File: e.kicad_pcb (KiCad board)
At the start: 2 copper layers, 78 x 58.5 mm, 9 parts, among them SW1 usr, SW2 rst, U1 Display_ST7789, U2 MAX98357A

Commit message: final changes, yay!
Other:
- board size 78 x 58.5 mm -> 78 x 58.3 mm
- board text added: "from monty X3"
- board text added: "text here"
- board text removed: "made by montypythonist X3"
- board text removed: "some notes: insert words here :)"
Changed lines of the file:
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@@
 		(at 166.45 98.31 90)
 		(property "Reference" "U1"
-			(at 0 -1.6 90)
+			(at -23.19 19.55 0)
 			(unlocked yes)
 			(layer "F.SilkS")
@@
 		(attr smd)
 		(duplicate_pad_numbers_are_jumpers no)
-		(fp_rect
-			(start -21.85 -21)
-			(end 21.85 20.8)
+		(fp_line
+			(start 21.844 -21)
+			(end 21.336 -21)
 			(stroke
 				(width 0.1)
-				(type solid)
+				(type default)
+			)
+			(layer "F.SilkS")
+		)
+		(fp_line
+			(start 21.844 -21)
+			(end 21.844 -20.492)
+			(stroke
+				(width 0.1)
+				(type default)
+			)
+			(layer "F.SilkS")
+		)
+		(fp_line
+			(start -21.844 20.828)
+			(end -21.844 20.32)
+			(stroke
+				(width 0.1)
+				(type default)
+			)
+			(layer "F.SilkS")
+		)
+		(fp_line
+			(start -21.844 20.828)
+			(end -21.336 20.828)
+			(stroke
+				(width 0.1)
+				(type default)
 			)
-			(fill no)
 			(layer "F.SilkS")
 		)
@@
 		(at 127.65 88.35 90)
 		(property "Reference" "LS1"
-			(at 14.7 -7 180)
+			(at 12.85 10.85 90)
 			(unlocked yes)
 			(layer "F.SilkS")
@@
 	(gr_rect
 		(start 112.15 66.15)
-		(end 190.15 124.650001)
+		(end 190.15 124.499999)
 		(stroke
 			(width 0.05)
@@
 	)
 	(gr_text "this routing haunts me in my sleep"
-		(at 189.15 109.65 90)
+		(at 188.5 111 90)
 		(layer "F.SilkS")
 		(effects
 			(font
-				(size 0.5 0.5)
+				(size 0.7 0.7)
 				(thickness 0.1)
 				(bold yes)
@@
 	)
 	(gr_text "on"
-		(at 135.649999 70.473333 90)
+		(at 136 71 90)
 		(layer "F.SilkS")
 		(effects
 			(font
-				(size 0.7 0.7)
+				(size 0.8 0.8)
 				(thickness 0.1)
 				(bold yes)
@@
 	)
 	(gr_text "off"
-		(at 122.649999 69.473333 270)
+		(at 122 69.5 270)
 		(layer "F.SilkS")
 		(effects
 			(font
-				(size 0.7 0.7)
+				(size 0.8 0.8)
 				(thickness 0.1)
 				(bold yes)
@@
 		)
 	)
-	(gr_text "made by\nmontypythonist X3"
-		(at 113.65 74.15 270)
+	(gr_text "from monty X3"
+		(at 113.5 67.5 270)
 		(layer "F.SilkS")
 		(effects
@@
 				(thickness 0.1)
 			)
-			(justify bottom)
+			(justify left bottom)
 		)
 	)
-	(gr_text "some notes: \ninsert words here :)"
+	(gr_text "text here"
 		(at 117.15 123.65 90)
 		(layer "F.SilkS")
@@
 		)
 	)
-	(group ""
-		(members "b0904ed2-5f99-419c-b382-4dc33d7675e0")
-	)
-	(group ""
-		(members "44044c4c-9110-4a88-b0ce-294c61a6f578")
-	)
-	(group ""
-		(members "03bbb989-da97-4d1e-8210-7c8b60939a85" "ce20f35f-f039-4fc7-9ab9-af98ebee2966")
-	)
 	(embedded_fonts no)

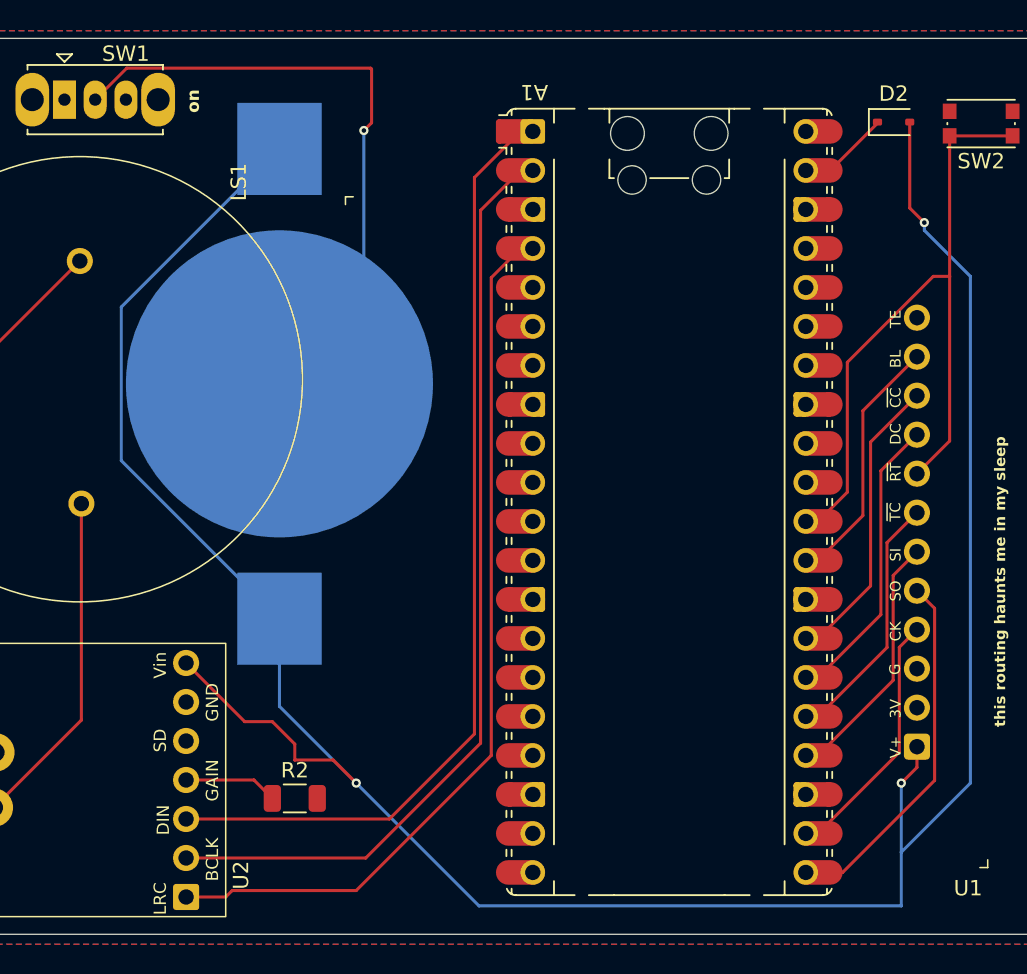
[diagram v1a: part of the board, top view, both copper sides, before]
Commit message: minor schematic cosmetic changes, cleaned up a few traces on PCB
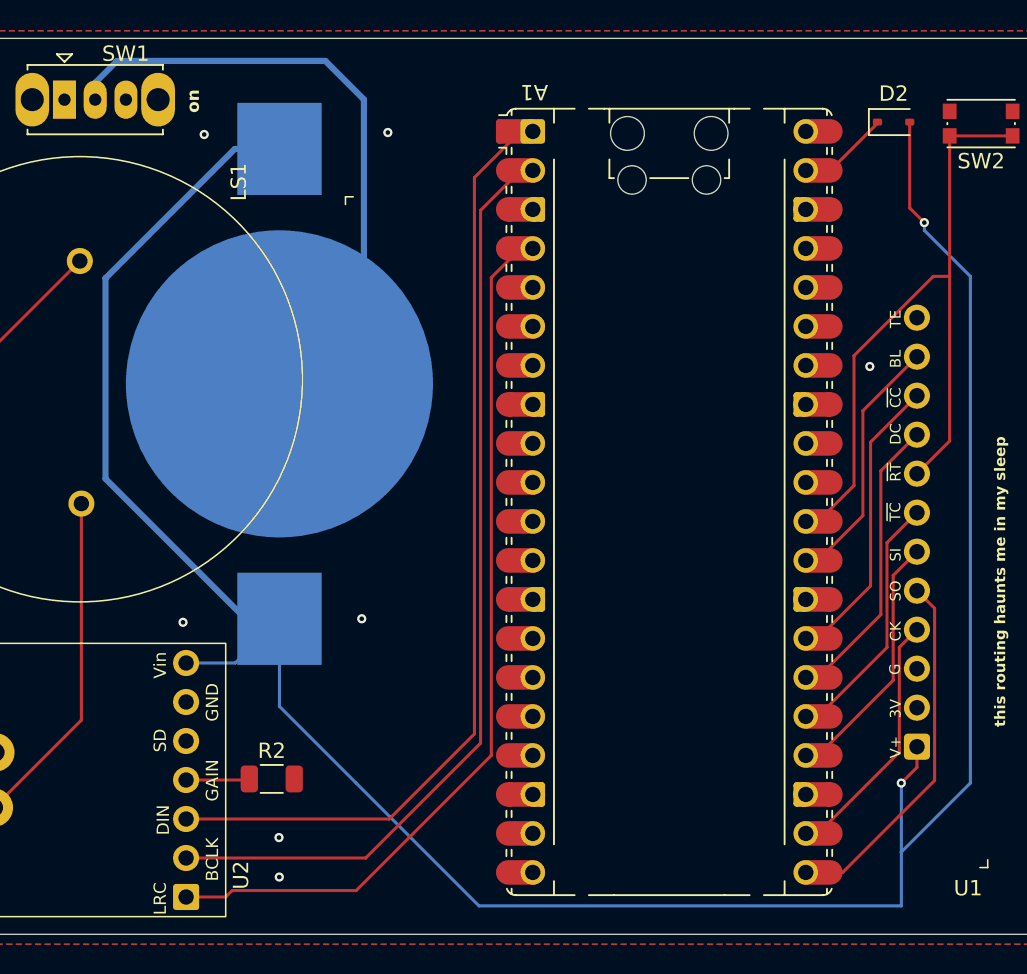
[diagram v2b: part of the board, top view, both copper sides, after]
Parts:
- moved R2 1.97 mm to (140.7, 114.4)
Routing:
- net +3V0: track 167.5 -> 163.7 mm, vias 3 -> 2
- net Net-(U2-GAIN_SLOT): track 6.11 -> 4.15 mm
- net Net-(BT1--): track 45.4 -> 44.6 mm, vias 1 -> 0
- net GND: vias 0 -> 7
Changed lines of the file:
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@@
 	(footprint "Resistor_SMD:R_1206_3216Metric"
 		(layer "F.Cu")
-		(at 142.15 115.65)
+		(at 140.65 114.38)
 		(descr "Resistor SMD 1206 (3216 Metric), square (rectangular) end terminal, IPC-7351 nominal, (Body size source: IPC-SM-782 page 72, https://www.pcb-3d.com/wordpress/wp-content/uploads/ipc-sm-782a_amendment_1_and_2.pdf)")
 		(tags "resistor")
@@
 			)
 		)
-		(property "Description" "Switch, single pole double throw"
+		(property "Description" "Switch, single pole double throw, keystone"
 			(at 0 0 0)
 			(unlocked yes)
@@
 			)
 		)
-		(property "Datasheet" ""
+		(property "Datasheet" "https://cdn-shop.adafruit.com/product-files/3787/3787_tft_QT154H2201__________20190228182902.pdf"
 			(at 0 0 90)
 			(unlocked yes)
@@
 		(sheetname "/")
 		(sheetfile "e.kicad_sch")
+		(units
+			(unit
+				(name "A")
+				(pins "4" "6" "7" "8" "9" "10" "11" "1" "3" "2" "5")
+			)
+		)
 		(attr smd)
 		(duplicate_pad_numbers_are_jumpers no)
@@
 			)
 		)
-		(attr smd)
+		(attr smd exclude_from_bom dnp)
 		(duplicate_pad_numbers_are_jumpers no)
 		(fp_line
@@
 				(name "A")
 				(pins "30" "37" "1" "2" "4" "5" "6" "7" "9" "10" "11" "12" "14" "15"
-					"16" "17" "19" "20" "39" "40" "18" "23" "28" "13" "8" "38" "3" "36"
+					"16" "17" "19" "20" "39" "40" "23" "3" "8" "38" "13" "28" "18" "36"
 					"21" "22" "24" "25" "26" "27" "29" "35" "31" "32" "34" "33"
 				)
@@
 		(start 112.15 66.15)
 		(end 190.15 124.499999)
+		(radius 1)
 		(stroke
 			(width 0.05)
@@
 	)
 	(segment
-		(start 139.4875 114.45)
+		(start 139.1175 114.45)
 		(end 135.07 114.45)
 		(width 0.2)
@@
 	)
 	(segment
-		(start 140.6875 115.65)
-		(end 139.4875 114.45)
+		(start 139.1875 114.38)
+		(end 139.1175 114.45)
 		(width 0.2)
 		(layer "F.Cu")
 		(net "Net-(U2-GAIN_SLOT)")
 	)
-	(segment
-		(start 147.15 68.15)
-		(end 147.15 71.65)
-		(width 0.2)
-		(layer "F.Cu")
-		(net "Net-(BT1--)")
+	(via
+		(at 141.12 118.2)
+		(size 0.6)
+		(drill 0.3)
+		(layers "F.Cu" "B.Cu")
+		(free yes)
+		(net "GND")
 	)
-	(segment
-		(start 147.15 71.65)
-		(end 146.65 72.15)
-		(width 0.2)
-		(layer "F.Cu")
-		(net "Net-(BT1--)")
+	(via
+		(at 136.25 72.41)
+		(size 0.6)
+		(drill 0.3)
+		(layers "F.Cu" "B.Cu")
+		(free yes)
+		(net "GND")
 	)
-	(segment
-		(start 147.09 68.09)
-		(end 147.15 68.15)
-		(width 0.2)
-		(layer "F.Cu")
-		(net "Net-(BT1--)")
+	(via
+		(at 141.14 120.77)
+		(size 0.6)
+		(drill 0.3)
+		(layers "F.Cu" "B.Cu")
+		(free yes)
+		(net "GND")
 	)
-	(segment
-		(start 129.15 70.14)
-		(end 131.2 68.09)
-		(width 0.2)
-		(layer "F.Cu")
-		(net "Net-(BT1--)")
+	(via
+		(at 148.21 72.28)
+		(size 0.6)
+		(drill 0.3)
+		(layers "F.Cu" "B.Cu")
+		(free yes)
+		(net "GND")
 	)
-	(segment
-		(start 131.2 68.09)
-		(end 147.09 68.09)
-		(width 0.2)
-		(layer "F.Cu")
-		(net "Net-(BT1--)")
+	(via
+		(at 134.87 104.18)
+		(size 0.6)
+		(drill 0.3)
+		(layers "F.Cu" "B.Cu")
+		(free yes)
+		(net "GND")
 	)
 	(via
-		(at 146.65 72.15)
+		(at 179.6 87.52)
 		(size 0.6)
 		(drill 0.3)
 		(layers "F.Cu" "B.Cu")
+		(free yes)
+		(net "GND")
+	)
+	(via
+		(at 146.51 103.95)
+		(size 0.6)
+		(drill 0.3)
+		(layers "F.Cu" "B.Cu")
+		(free yes)
+		(net "GND")
+	)
+	(segment
+		(start 146.65 70.13)
+		(end 144.14 67.62)
+		(width 0.4)
+		(layer "B.Cu")
 		(net "Net-(BT1--)")
 	)
 	(segment
-		(start 146.65 72.15)
+		(start 146.65 83.15)
+		(end 146.65 70.13)
+		(width 0.4)
+		(layer "B.Cu")
+		(net "Net-(BT1--)")
+	)
+	(segment
+		(start 130.57 67.62)
+		(end 129.15 69.04)
+		(width 0.4)
+		(layer "B.Cu")
+		(net "Net-(BT1--)")
+	)
+	(segment
+		(start 141.15 88.65)
 		(end 146.65 83.15)
-		(width 0.2)
+		(width 0.4)
 		(layer "B.Cu")
 		(net "Net-(BT1--)")
@@
 	)
 	(segment
-		(start 146.65 83.15)
-		(end 141.15 88.65)
-		(width 0.2)
+		(start 129.15 69.04)
+		(end 129.15 70.14)
+		(width 0.4)
 		(layer "B.Cu")
 		(net "Net-(BT1--)")
 	)
 	(segment
-		(start 182.67 113.63)
-		(end 181.65 114.65)
-		(width 0.2)
-		(layer "F.Cu")
-		(net "+3V0")
+		(start 144.14 67.62)
+		(end 130.57 67.62)
+		(width 0.4)
+		(layer "B.Cu")
+		(net "Net-(BT1--)")
 	)
 	(segment
-		(start 142.15 113.15)
-		(end 142.15 112.1125)
+		(start 182.67 113.63)
+		(end 181.65 114.65)
 		(width 0.2)
 		(layer "F.Cu")
@@
 	)
 	(segment
-		(start 144.65 113.15)
-		(end 142.15 113.15)
-		(width 0.2)
-		(layer "F.Cu")
-		(net "+3V0")
-	)
-	(segment
-		(start 142.15 112.1125)
-		(end 140.6875 110.65)
-		(width 0.2)
-		(layer "F.Cu")
-		(net "+3V0")
-	)
-	(segment
 		(start 182.67 112.28)
 		(end 182.67 113.63)
@@
 	)
 	(segment
-		(start 146.15 114.65)
-		(end 144.65 113.15)
-		(width 0.2)
-		(layer "F.Cu")
-		(net "+3V0")
-	)
-	(segment
-		(start 135.07 106.83)
-		(end 138.89 110.65)
-		(width 0.2)
-		(layer "F.Cu")
-		(net "+3V0")
-	)
-	(segment
 		(start 182.2 77.2)
 		(end 183.15 78.15)
@@
 		(net "+3V0")
 	)
-	(segment
-		(start 138.89 110.65)
-		(end 140.6875 110.65)
-		(width 0.2)
-		(layer "F.Cu")
-		(net "+3V0")
-	)
-	(via
-		(at 146.15 114.65)
-		(size 0.6)
-		(drill 0.3)
-		(layers "F.Cu" "B.Cu")
-		(net "+3V0")
-	)
 	(via
 		(at 181.65 114.65)
@@
 	)
 	(segment
+		(start 138.24 73.35)
+		(end 141.15 73.35)
+		(width 0.4)
+		(layer "B.Cu")
+		(net "+3V0")
+	)
+	(segment
 		(start 186.15 114.65)
 		(end 181.65 119.15)
@@
 	)
 	(segment
+		(start 138.94 103.95)
+		(end 129.82 94.83)
+		(width 0.4)
+		(layer "B.Cu")
+		(net "+3V0")
+	)
+	(segment
+		(start 129.82 94.83)
+		(end 129.82 81.77)
+		(width 0.4)
+		(layer "B.Cu")
+		(net "+3V0")
+	)
+	(segment
 		(start 183.15 78.15)
 		(end 183.15 78.65)
@@
 	)
 	(segment
-		(start 130.85 93.65)
-		(end 130.85 83.65)
-		(width 0.2)
+		(start 141.15 103.95)
+		(end 138.94 103.95)
+		(width 0.4)
 		(layer "B.Cu")
 		(net "+3V0")
 	)
 	(segment
-		(start 130.85 83.65)
-		(end 141.15 73.35)
+		(start 135.07 106.83)
+		(end 138.27 106.83)
 		(width 0.2)
 		(layer "B.Cu")
@@
 	)
 	(segment
-		(start 154.15 122.65)
-		(end 146.15 114.65)
+		(start 138.27 106.83)
+		(end 141.15 103.95)
 		(width 0.2)
 		(layer "B.Cu")
@@
 	)
 	(segment
-		(start 186.15 81.65)
-		(end 186.15 114.65)
+		(start 129.82 81.77)
+		(end 138.24 73.35)
+		(width 0.4)
+		(layer "B.Cu")
+		(net "+3V0")
+	)
+	(segment
+		(start 154.15 122.65)
+		(end 146.15 114.65)
 		(width 0.2)
 		(layer "B.Cu")
@@
 	)
 	(segment
-		(start 141.15 103.95)
-		(end 130.85 93.65)
+		(start 186.15 81.65)
+		(end 186.15 114.65)
 		(width 0.2)
 		(layer "B.Cu")
@@
 	)
 	(segment
-		(start 178.135 87.248654)
-		(end 178.135 95.705)
+		(start 178.57 86.813654)
+		(end 178.57 95.27)
 		(width 0.2)
 		(layer "F.Cu")
@@
 	)
 	(segment
-		(start 184.8 81.65)
-		(end 183.733654 81.65)
+		(start 178.57 95.27)
+		(end 176.23 97.61)
 		(width 0.2)
 		(layer "F.Cu")
@@
 	)
 	(segment
-		(start 178.135 95.705)
-		(end 176.23 97.61)
+		(start 183.733654 81.65)
+		(end 178.57 86.813654)
 		(width 0.2)
 		(layer "F.Cu")
@@
 	)
 	(segment
-		(start 183.733654 81.65)
-		(end 178.135 87.248654)
+		(start 184.8 81.65)
+		(end 183.733654 81.65)
 		(width 0.2)
 		(layer "F.Cu")

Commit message: NOW its done fr yay time 4 codeing
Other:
- board text added: "happy birthday jake!!"
- board text removed: "text here"
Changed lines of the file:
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@@
 		)
 	)
-	(gr_text "text here"
-		(at 117.15 123.65 90)
+	(gr_text "happy birthday jake!!"
+		(at 115.5 123 90)
 		(layer "F.SilkS")
 		(effects

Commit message: pcb layout done!!
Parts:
- A1: footprint Module:RaspberryPi_Pico_Common_Unspecified -> Module:RaspberryPi_Pico_Common_SMD
- BT1: value CR2430 -> CR2450
- D2: footprint Diode_SMD:D_SOD-323 -> Diode_SMD:D_SOD-128
- R2: footprint Resistor_SMD:R_1206_3216Metric -> Resistor_SMD:R_1812_4532Metric
- SW2: footprint Button_Switch_SMD:SW_Push_1P1T_NO_CK_KMR2 -> Button_Switch_SMD:SW_Push_SPST_NO_Alps_SKRK
- moved SW1 136.5 mm to (260.0, 101.3), turned to 90 degrees
- moved BT1 87.9 mm to (228.0, 102.5), turned to 90 degrees
- moved U2 85.9 mm to (213.1, 127.4)
- moved SW2 84.1 mm to (260.5, 112.3), turned to 90 degrees
- moved D2 81.1 mm to (261.0, 86.0), turned to -90 degrees
- moved A1 76.6 mm to (242.6, 105.0)
- moved R2 69.4 mm to (210.0, 114.0), turned to 90 degrees
- moved LS1 62.2 mm to (186.5, 108.4)
- moved U1 46.9 mm to (202.0, 67.8), turned to 0 degrees
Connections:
- A1 pad 10: unconnected-(A1-GPIO7-Pad10) -> Net-(A1-GPIO7)
- A1 pad 17: unconnected-(A1-GPIO13-Pad17) -> Net-(A1-GPIO13)
- A1 pad 19: unconnected-(A1-GPIO14-Pad19)_1 -> Net-(A1-GPIO14)
- A1 pad 20: unconnected-(A1-GPIO15-Pad20)_1 -> Net-(A1-GPIO15)
- A1 pad 21: Net-(A1-GPIO16) -> unconnected-(A1-GPIO16-Pad21)
- A1 pad 22: Net-(A1-GPIO17) -> unconnected-(A1-GPIO17-Pad22)
- A1 pad 24: Net-(A1-GPIO18) -> unconnected-(A1-GPIO18-Pad24)
- A1 pad 25: Net-(A1-GPIO19) -> unconnected-(A1-GPIO19-Pad25)
- A1 pad 26: Net-(A1-GPIO20) -> unconnected-(A1-GPIO20-Pad26)
- A1 pad 27: Net-(A1-GPIO21) -> unconnected-(A1-GPIO21-Pad27)
- A1 pad 29: Net-(A1-GPIO22) -> unconnected-(A1-GPIO22-Pad29)
- A1 pad 33: unconnected-(A1-AGND-Pad33) -> GND
- A1 pad 36: unconnected-(A1-3V3-Pad36)_1 -> PICO_PWR
- A1 pad 5: unconnected-(A1-GPIO3-Pad5) -> Net-(A1-GPIO3)
- A1 pad 6: unconnected-(A1-GPIO4-Pad6) -> Net-(A1-GPIO4)
- A1 pad 7: unconnected-(A1-GPIO5-Pad7) -> Net-(A1-GPIO5)
- A1 pad 9: unconnected-(A1-GPIO6-Pad9)_1 -> Net-(A1-GPIO6)
- BT1 pad 1: +3V0 -> Net-(BT1-+)
- BT1 pad 2: Net-(BT1--) -> GND
- SW1 pad 1: GND -> Net-(BT1-+)
- SW1 pad 2: Net-(BT1--) -> +3V0
- SW2 pad 1: Net-(A1-RUN) -> GND
- SW2 pad 2: GND -> Net-(A1-RUN)
- U1 pad 1: +3V0 -> PICO_PWR
- U1 pad 10: Net-(A1-GPIO21) -> Net-(A1-GPIO2)
- U1 pad 11: Net-(A1-GPIO22) -> Net-(A1-GPIO1)
- U1 pad 4: Net-(A1-GPIO17) -> Net-(A1-GPIO7)
- U1 pad 5: Net-(A1-GPIO16) -> Net-(A1-GPIO0)
- U1 pad 6: Net-(A1-GPIO18) -> Net-(A1-GPIO6)
- U1 pad 7: Net-(A1-GPIO19) -> Net-(A1-GPIO5)
- U1 pad 8: Net-(A1-RUN) -> Net-(A1-GPIO4)
- U1 pad 9: Net-(A1-GPIO20) -> Net-(A1-GPIO3)
- U2 pad 1: Net-(A1-GPIO2) -> Net-(A1-GPIO15)
- U2 pad 2: Net-(A1-GPIO1) -> Net-(A1-GPIO14)
- U2 pad 3: Net-(A1-GPIO0) -> Net-(A1-GPIO13)
- U2 pad 7: +3V0 -> PICO_PWR
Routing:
- net +3V0: track 163.7 -> 12.4 mm, vias 2 -> 0
- net PICO_PWR: track 0.00 -> 93.5 mm
- net Net-(BT1-+): track 0.00 -> 78.0 mm, vias 0 -> 1
- net Net-(A1-GPIO7): track 0.00 -> 45.4 mm
- net Net-(BT1--): track 44.6 -> 0.00 mm
- net Net-(A1-GPIO6): track 0.00 -> 41.2 mm
- net Net-(A1-GPIO1): track 60.7 -> 20.7 mm
- net Net-(A1-RUN): track 47.1 -> 9.82 mm
- net Net-(A1-GPIO5): track 0.00 -> 34.6 mm
- net Net-(A1-GPIO2): track 57.5 -> 23.9 mm
- net Net-(A1-GPIO4): track 0.00 -> 31.0 mm
- net Net-(A1-GPIO3): track 0.00 -> 27.5 mm
- net Net-(A1-GPIO0): track 61.6 -> 36.0 mm
- net Net-(A1-GPIO16): track 22.9 -> 0.00 mm
- net Net-(A1-GPIO21): track 18.5 -> 0.00 mm
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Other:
- board size 78 x 58.3 mm -> 80 x 58.5 mm
- board text removed: "from monty X3"
- board text removed: "happy birthday jake!!"
- board text removed: "this routing haunts me in my sleep"

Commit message: gerber files made, yay!
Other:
- board text added: "<ö>"
- board text added: "from monty :)"

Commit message: edited page stuff
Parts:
- moved A1 79.9 mm to (162.8, 100.3)
- moved BT1 79.9 mm to (148.2, 97.8)
- moved D2 79.9 mm to (181.2, 81.3)
- moved LS1 79.9 mm to (106.7, 103.7)
- moved R2 79.9 mm to (130.2, 109.3)
- moved SW1 79.9 mm to (180.2, 96.6)
- moved SW2 79.9 mm to (180.7, 107.6)
- moved U1 79.9 mm to (122.2, 63.1)
- moved U2 79.9 mm to (133.3, 122.7)

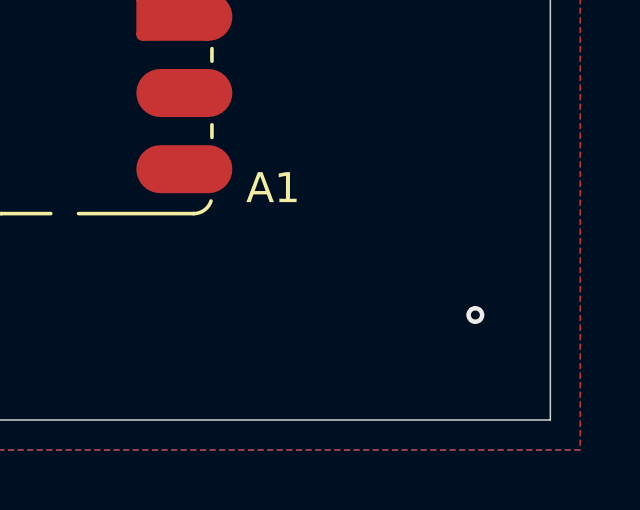
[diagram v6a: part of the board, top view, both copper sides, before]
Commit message: silkscreen watermark placeholder for pcbway or something like that
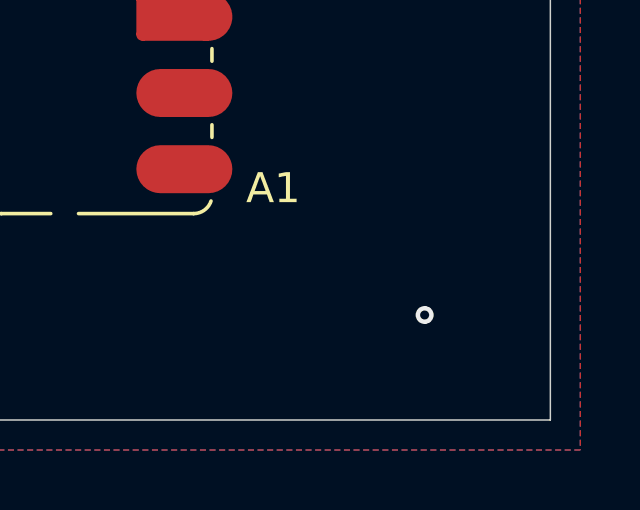
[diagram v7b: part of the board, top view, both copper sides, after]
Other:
- board text added: "WayWayWay"
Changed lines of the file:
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@@
+		)
+	)
+	(gr_text "WayWayWay"
+		(at 183 131 90)
+		(layer "B.SilkS")
+		(effects
+			(font
+				(size 1.5 1.5)
+				(thickness 0.3)
+				(bold yes)
+			)
+			(justify left bottom)
 		)
 	)
@@
 	)
 	(via
-		(at 182.19 129.3)
+		(at 180.5 129.3)
 		(size 0.6)
 		(drill 0.3)

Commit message: mfw i cant find one part so i have to change the entire board
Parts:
- R2: footprint Resistor_SMD:R_1812_4532Metric -> Resistor_THT:R_Axial_DIN0207_L6.3mm_D2.5mm_P10.16mm_Horizontal
- SW2: footprint Button_Switch_SMD:SW_Push_SPST_NO_Alps_SKRK -> Button_Switch_THT:SW_PUSH_6mm
- moved SW2 4.47 mm to (178.5, 111.5)
- moved R2 2.50 mm to (129.0, 111.5)
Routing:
- net Net-(A1-RUN): track 9.82 -> 18.4 mm
- net PICO_PWR: track 93.5 -> 94.1 mm
- net GND: vias 15 -> 14
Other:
- board size 80 x 58.5 mm -> 80.8 x 58.5 mm
